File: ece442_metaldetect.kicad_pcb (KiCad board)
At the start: 2 copper layers, 35 parts, among them J4 Conn_01x08_Male, M1 Motor_DC, U4 74LS86

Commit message: Add files via upload
the actual changes made
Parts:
- removed C11: 100n, Capacitor_SMD:C_0402_1005Metric
- added J1: 1-2834011-2, TestPoint:connect_detect, F.Cu at (99.1, 104.1)
- added J2: 1-2834011-2, TestPoint:connect_detect, F.Cu at (88.9, 104.1)
- added J3: Conn_01x03_Male, Connector_PinHeader_2.54mm:PinHeader_1x03_P2.54mm_Horizontal, F.Cu at (160.7, 111.8)
- added J5: Screw_Terminal_01x02, Connector_PinHeader_2.54mm:PinHeader_1x02_P2.54mm_Vertical, F.Cu at (114.3, 104.1)
- added J6: Screw_Terminal_01x02, Connector_PinHeader_2.54mm:PinHeader_1x02_P2.54mm_Vertical, F.Cu at (104.1, 121.9)
- added U1: LM1458N, TestPoint:DIP794-detect, B.Cu at (109.2, 114.3)
- added U2: LMC6032IMX/NOPB, TestPoint:SOIC127P599X175-8N, B.Cu at (142.2, 116.8)
- added U3: LMC6032IMX/NOPB, TestPoint:SOIC127P599X175-8N, B.Cu at (128.3, 111.8)
- C1, C2, D1, D2, R1, R10, R11, R12, R13, R14, R15, R16, R2, R3, R4, R5, R6, R7, R8, R9, U4: moved to B.Cu
- C10, C12, C3, C4, C5, C6, C7, C8, C9: footprint Capacitor_SMD:C_0402_1005Metric -> Capacitor_SMD:C_0805_2012Metric; moved to B.Cu
- M1: footprint libraries:VCLP0820B004L_Vibrator -> TestPoint:vclp_vibrator
- moved C10 64.7 mm to (101.6, 114.3), turned to -90 degrees
- moved J4 57.2 mm to (83.1, 123.2), turned to 180 degrees
- moved C7 56.9 mm to (88.9, 109.2), turned to -90 degrees
- moved M1 51.9 mm to (96.5, 116.8)
- moved R9 51.0 mm to (109.2, 116.8), turned to -90 degrees
- moved A1 46.7 mm to (114.3, 121.9), turned to 90 degrees
- moved R4 46.3 mm to (99.1, 109.2), turned to 180 degrees
- moved R15 45.5 mm to (116.8, 119.4), turned to 180 degrees
- moved D2 45.3 mm to (123.2, 116.8), turned to 180 degrees
- moved C1 39.9 mm to (91.4, 121.9), turned to 180 degrees
- moved C9 38.4 mm to (134.6, 116.8), turned to -90 degrees
- moved C8 36.2 mm to (137.2, 116.8), turned to 90 degrees
- moved R2 36.1 mm to (121.9, 114.3), turned to 180 degrees
- moved R12 32.8 mm to (144.8, 111.8), turned to 90 degrees
- moved U4 32.6 mm to (151.1, 114.3), turned to 90 degrees
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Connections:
- A1 pad 27: unconnected-(A1-Pad27) -> +5V
- A1 pad 29: unconnected-(A1-Pad29) -> GND
- A1 pad 4: unconnected-(A1-Pad4) -> GND
- C10 pad 1: unconnected-(C10-Pad1) -> +12V
- C10 pad 2: unconnected-(C10-Pad2) -> GND
- C12 pad 1: unconnected-(C12-Pad1) -> +5V
- C12 pad 2: unconnected-(C12-Pad2) -> GND
- C5 pad 1: unconnected-(C5-Pad1) -> +9V
- C5 pad 2: unconnected-(C5-Pad2) -> GND
- C6 pad 1: unconnected-(C6-Pad1) -> +12V
- C6 pad 2: unconnected-(C6-Pad2) -> GND
- C7 pad 1: unconnected-(C7-Pad1) -> +12V
- C7 pad 2: unconnected-(C7-Pad2) -> GND
- C8 pad 1: unconnected-(C8-Pad1) -> GND
- C8 pad 2: unconnected-(C8-Pad2) -> +5V
- C9 pad 1: unconnected-(C9-Pad1) -> +5V
- C9 pad 2: unconnected-(C9-Pad2) -> GND
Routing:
- net GND: track 0.00 -> 259.0 mm, vias 0 -> 10
- net /ReferenceSignalSquare: track 0.00 -> 123.9 mm
- net +5V: track 0.00 -> 121.9 mm, vias 0 -> 3
- net /Sin12.0Vpp: track 0.00 -> 121.5 mm, vias 0 -> 3
- net /rxSignalSquare: track 0.00 -> 103.6 mm, vias 0 -> 2
- net /PhaseShiftSquareWave: track 0.00 -> 94.0 mm, vias 0 -> 5
- net /RXSinWave: track 0.00 -> 93.3 mm, vias 0 -> 3
- net +12V: track 0.00 -> 74.2 mm, vias 0 -> 5
- net GNDREF: track 0.00 -> 58.8 mm, vias 0 -> 6
- net +9V: track 0.00 -> 41.3 mm, vias 0 -> 1
- net /OP1IN+2: track 0.00 -> 35.1 mm
- net Net-(C4-Pad2): track 0.00 -> 25.3 mm, vias 0 -> 2
- net /OP1IN-2: track 0.00 -> 23.6 mm
- net /Sin1.4Vpp: track 0.00 -> 22.1 mm, vias 0 -> 2
- net Net-(M1-Pad1): track 0.00 -> 16.4 mm, vias 0 -> 1
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- added copper zone on B.Cu, net GND
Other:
- board outline added: 81.3 x 25.4 mm

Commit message: Add files via upload
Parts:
- moved J5 5.08 mm to (109.2, 104.1)
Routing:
- net GND: track 259.0 -> 253.7 mm
- net +9V: track 41.3 -> 39.6 mm
- removed copper zone on B.Cu, net GND
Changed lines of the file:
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@@
     (property "Sheetname" "")
     (attr through_hole)
-    (fp_text reference "J4" (at 4.385 -2.27) (layer "F.SilkS")
+    (fp_text reference "J4" (at -0.705 -2.27) (layer "F.SilkS")
       (effects (font (size 1 1) (thickness 0.15)))
     )
@@
     (property "Sheetname" "")
     (attr through_hole)
-    (fp_text reference "J3" (at 4.385 -2.27) (layer "F.SilkS")
+    (fp_text reference "J3" (at -0.705 -2.54) (layer "F.SilkS")
       (effects (font (size 1 1) (thickness 0.15)))
     )
@@
     (property "Sheetname" "")
     (attr through_hole)
-    (fp_text reference "A1" (at 5.08 40.64 90) (layer "B.SilkS")
+    (fp_text reference "A1" (at -0.01 40.64 180) (layer "B.SilkS")
       (effects (font (size 1 1) (thickness 0.15)) (justify mirror))
     )
@@
       (effects (font (size 1 1) (thickness 0.15)))
     )
-    (fp_text user "${REFERENCE}" (at 6.35 36.83) (layer "F.Fab")
+    (fp_text user "${REFERENCE}" (at -1.27 40.64) (layer "F.Fab")
       (effects (font (size 1 1) (thickness 0.15)))
     )
@@
   )
   (footprint "Connector_PinHeader_2.54mm:PinHeader_1x02_P2.54mm_Vertical" (layer "F.Cu")
-    (at 114.3 104.14 90)
+    (at 109.22 104.14 90)
     (descr "Through hole straight pin header, 1x02, 2.54mm pitch, single row")
     (tags "Through hole pin header THT 1x02 2.54mm single row")
@@
       (effects (font (size 1 1) (thickness 0.15)))
     )
-    (fp_text user "${REFERENCE}" (at 0 1.27) (layer "F.Fab")
+    (fp_text user "${REFERENCE}" (at -2.54 1.27) (layer "F.Fab")
       (effects (font (size 1 1) (thickness 0.15)))
     )
@@
     (property "Sheetname" "")
     (attr smd)
-    (fp_text reference "C12" (at 0 1.68) (layer "B.SilkS")
+    (fp_text reference "C12" (at 2.54 0) (layer "B.SilkS")
       (effects (font (size 1 1) (thickness 0.15)) (justify mirror))
     )
@@
     (property "Sheetname" "")
     (attr smd)
-    (fp_text reference "R2" (at 0 1.43) (layer "B.SilkS")
+    (fp_text reference "R2" (at -2.54 0) (layer "B.SilkS")
       (effects (font (size 1 1) (thickness 0.15)) (justify mirror))
     )
@@
     (property "Sheetname" "")
     (attr smd)
-    (fp_text reference "R4" (at 0 1.82) (layer "B.SilkS")
+    (fp_text reference "R4" (at -2.54 1.82) (layer "B.SilkS")
       (effects (font (size 1 1) (thickness 0.15)) (justify mirror))
     )
@@
     (property "Sheetname" "")
     (attr smd)
-    (fp_text reference "C5" (at 0 1.68 90) (layer "B.SilkS")
+    (fp_text reference "C5" (at -0.261252 -2.54 90) (layer "B.SilkS")
       (effects (font (size 1 1) (thickness 0.15)) (justify mirror))
     )
@@
     (property "Sheetname" "")
     (attr smd)
-    (fp_text reference "C8" (at 0 1.68 90) (layer "B.SilkS")
+    (fp_text reference "C8" (at 2.54 0 90) (layer "B.SilkS")
       (effects (font (size 1 1) (thickness 0.15)) (justify mirror))
     )
@@
     (property "Sheetname" "")
     (attr smd)
-    (fp_text reference "R8" (at 0 1.65 90) (layer "B.SilkS")
+    (fp_text reference "R8" (at -2.54 0 90) (layer "B.SilkS")
       (effects (font (size 1 1) (thickness 0.15)) (justify mirror))
     )
@@
     (property "Sheetname" "")
     (attr smd)
-    (fp_text reference "R7" (at 0 1.82 90) (layer "B.SilkS")
+    (fp_text reference "R7" (at 2.54 1.82 90) (layer "B.SilkS")
       (effects (font (size 1 1) (thickness 0.15)) (justify mirror))
     )
@@
     (property "Sheetname" "")
     (attr smd)
-    (fp_text reference "R12" (at 0 1.65 90) (layer "B.SilkS")
+    (fp_text reference "R12" (at 2.54 2.54 90) (layer "B.SilkS")
       (effects (font (size 1 1) (thickness 0.15)) (justify mirror))
     )
@@
     (property "Sheetname" "")
     (attr smd)
-    (fp_text reference "R14" (at 0 1.65) (layer "B.SilkS")
+    (fp_text reference "R14" (at 2.54 0) (layer "B.SilkS")
       (effects (font (size 1 1) (thickness 0.15)) (justify mirror))
     )
@@
     (property "Sheetname" "")
     (attr through_hole)
-    (fp_text reference "C1" (at 2.5 3) (layer "B.SilkS")
+    (fp_text reference "C1" (at 2.5 -2.54) (layer "B.SilkS")
       (effects (font (size 1 1) (thickness 0.15)) (justify mirror))
     )
@@
     (property "Sheetname" "")
     (attr smd)
-    (fp_text reference "R3" (at 0 1.82) (layer "B.SilkS")
+    (fp_text reference "R3" (at -3.6175 0) (layer "B.SilkS")
       (effects (font (size 1 1) (thickness 0.15)) (justify mirror))
     )
@@
     (property "Sheetname" "")
     (attr smd)
-    (fp_text reference "C9" (at 0 1.68 90) (layer "B.SilkS")
+    (fp_text reference "C9" (at 2.54 0 90) (layer "B.SilkS")
       (effects (font (size 1 1) (thickness 0.15)) (justify mirror))
     )
@@
     (property "Sheetname" "")
     (attr smd)
-    (fp_text reference "R1" (at 0 1.65) (layer "B.SilkS")
+    (fp_text reference "R1" (at 4.1675 0) (layer "B.SilkS")
       (effects (font (size 1 1) (thickness 0.15)) (justify mirror))
     )
@@
     (property "Sheetname" "")
     (attr smd)
-    (fp_text reference "R11" (at 0 1.65 90) (layer "B.SilkS")
+    (fp_text reference "R11" (at 2.54 0 90) (layer "B.SilkS")
       (effects (font (size 1 1) (thickness 0.15)) (justify mirror))
     )
@@
     (property "Sheetname" "")
     (attr smd)
-    (fp_text reference "C3" (at 0 1.68 90) (layer "B.SilkS")
+    (fp_text reference "C3" (at 2.54 0) (layer "B.SilkS")
       (effects (font (size 1 1) (thickness 0.15)) (justify mirror))
     )
@@
     (property "Sheetname" "")
     (attr smd)
-    (fp_text reference "C6" (at 0 1.68 90) (layer "B.SilkS")
+    (fp_text reference "C6" (at -2.54 0 90) (layer "B.SilkS")
       (effects (font (size 1 1) (thickness 0.15)) (justify mirror))
     )
@@
     (property "Sheetname" "")
     (attr through_hole)
-    (fp_text reference "U1" (at -3.105 4.872) (layer "B.SilkS")
+    (fp_text reference "U1" (at 0 5.08) (layer "B.SilkS")
       (effects (font (size 1 1) (thickness 0.15)) (justify mirror))
     )
@@
     (property "Sheetname" "")
     (attr smd)
-    (fp_text reference "U2" (at -0.385 3.537) (layer "B.SilkS")
+    (fp_text reference "U2" (at -5.08 -2.54) (layer "B.SilkS")
       (effects (font (size 1 1) (thickness 0.15)) (justify mirror))
     )
@@
     (property "Sheetname" "")
     (attr smd)
-    (fp_text reference "R15" (at 0 1.65) (layer "B.SilkS")
+    (fp_text reference "R15" (at -5.08 0) (layer "B.SilkS")
       (effects (font (size 1 1) (thickness 0.15)) (justify mirror))
     )
@@
   (segment (start 81.940489 124.349511) (end 84.465958 126.87498) (width 0.25) (layer "F.Cu") (net 4))
   (segment (start 99.18502 126.87498) (end 101.6 124.46) (width 0.25) (layer "F.Cu") (net 4))
-  (segment (start 116.84 106.67) (end 116.84 104.14) (width 0.25) (layer "F.Cu") (net 4))
   (segment (start 137.16 118.6555) (end 138.3968 119.8923) (width 0.25) (layer "F.Cu") (net 4))
   (segment (start 84.465958 126.87498) (end 99.18502 126.87498) (width 0.25) (layer "F.Cu") (net 4))
@@
   (segment (start 145.35 118.745) (end 144.71 118.745) (width 0.25) (layer "B.Cu") (net 4))
   (segment (start 107.085401 112.71) (end 105.473863 114.321538) (width 0.25) (layer "B.Cu") (net 4))
+  (segment (start 116.84 104.14) (end 111.76 104.14) (width 0.25) (layer "B.Cu") (net 4))
   (segment (start 161.899511 110.585489) (end 161.899511 113.125489) (width 0.25) (layer "B.Cu") (net 4))
   (segment (start 159.481206 110.585489) (end 161.899511 110.585489) (width 0.25) (layer "B.Cu") (net 4))
-  (segment (start 115.665489 102.965489) (end 106.904511 102.965489) (width 0.25) (layer "B.Cu") (net 4))
   (segment (start 105.73 104.14) (end 104.14 104.14) (width 0.25) (layer "B.Cu") (net 4))
   (segment (start 118.43 109.22) (end 116.84 109.22) (width 0.25) (layer "B.Cu") (net 4))
@@
   (segment (start 89.73 109.34) (end 88.9 110.17) (width 0.25) (layer "B.Cu") (net 4))
   (segment (start 109.22 112.71) (end 107.085401 112.71) (width 0.25) (layer "B.Cu") (net 4))
+  (segment (start 116.84 106.67) (end 116.84 104.14) (width 0.25) (layer "B.Cu") (net 4))
   (segment (start 137.16 117.79) (end 137.16 118.6555) (width 0.25) (layer "B.Cu") (net 4))
-  (segment (start 116.84 104.14) (end 115.665489 102.965489) (width 0.25) (layer "B.Cu") (net 4))
   (segment (start 117.7525 119.38) (end 118.20202 119.82952) (width 0.25) (layer "B.Cu") (net 5))
   (segment (start 118.20202 119.82952) (end 122.37952 119.82952) (width 0.25) (layer "B.Cu") (net 5))
@@
   (segment (start 95.377483 118.095) (end 104.177299 109.295184) (width 0.25) (layer "F.Cu") (net 29))
   (segment (start 83.115 118.095) (end 95.377483 118.095) (width 0.25) (layer "F.Cu") (net 29))
-  (segment (start 114.3 106.67) (end 114.3 104.14) (width 0.25) (layer "F.Cu") (net 29))
   (via (at 104.177299 106.642701) (size 0.8) (drill 0.4) (layers "F.Cu" "B.Cu") (net 29))
-  (segment (start 112.72 105.09) (end 114.3 106.67) (width 0.25) (layer "B.Cu") (net 29))
-  (segment (start 106.68 105.09) (end 112.72 105.09) (width 0.25) (layer "B.Cu") (net 29))
+  (segment (start 107.63 104.14) (end 109.22 104.14) (width 0.25) (layer "B.Cu") (net 29))
+  (segment (start 114.3 106.67) (end 111.75 106.67) (width 0.25) (layer "B.Cu") (net 29))
+  (segment (start 106.68 105.09) (end 107.63 104.14) (width 0.25) (layer "B.Cu") (net 29))
+  (segment (start 111.75 106.67) (end 109.22 104.14) (width 0.25) (layer "B.Cu") (net 29))
   (segment (start 104.177299 106.642701) (end 105.73 105.09) (width 0.25) (layer "B.Cu") (net 29))
   (segment (start 105.73 105.09) (end 106.68 105.09) (width 0.25) (layer "B.Cu") (net 29))
@@
   (segment (start 105.25 115.57) (end 106.52 114.3) (width 0.25) (layer "B.Cu") (net 49))
   (segment (start 109.38 114.3) (end 113.19 110.49) (width 0.25) (layer "B.Cu") (net 49))
-  (zone (net 4) (net_name "GND") (layer "B.Cu") (hatch edge 0.508)
-    (connect_pads (clearance 0.508))
-    (min_thickness 0.254) (filled_areas_thickness no)
-    (fill yes (thermal_gap 0.508) (thermal_bridge_width 0.508))
-    (polygon
-      (pts
-        (xy 162.56 127)
-        (xy 81.28 127)
-        (xy 81.28 101.6)
-        (xy 162.56 101.6)
-      )
-    )
-  )
 )

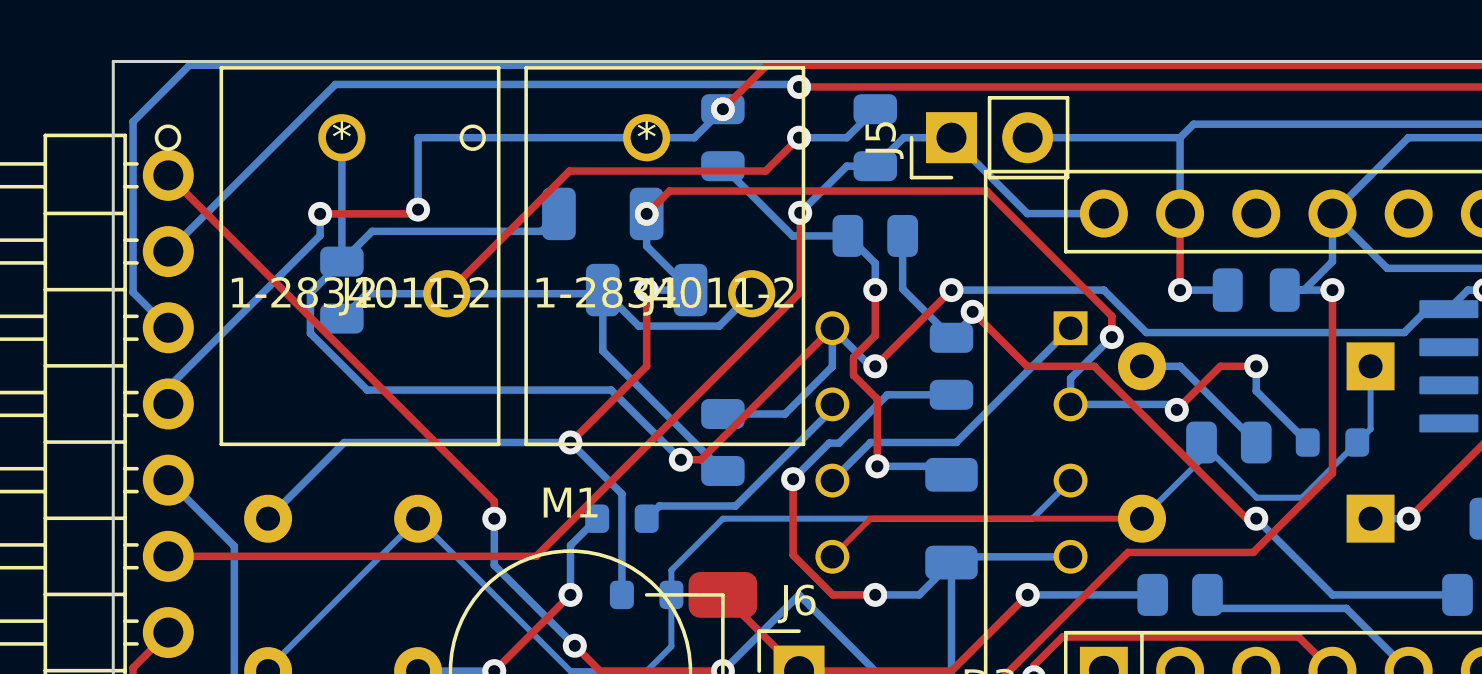
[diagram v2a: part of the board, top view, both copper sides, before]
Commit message: moved j5 and slikscreen labels to be more clear
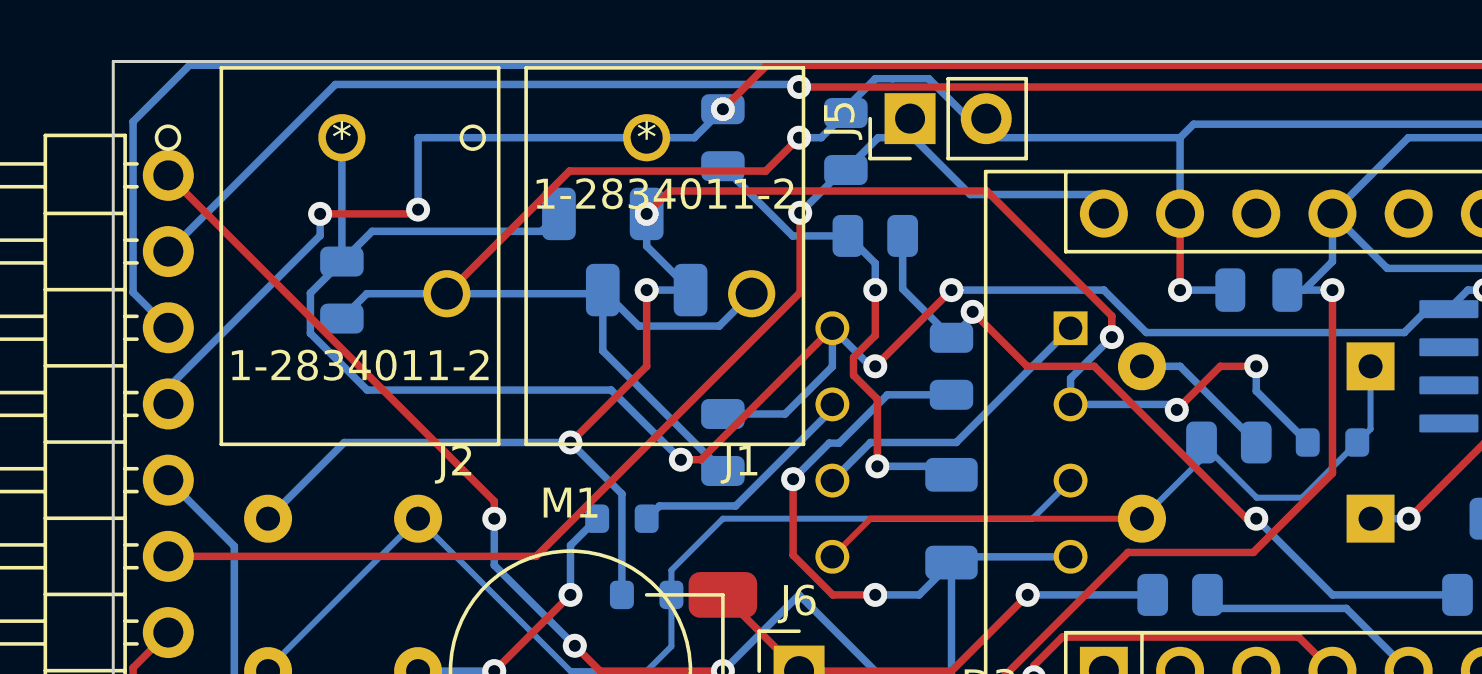
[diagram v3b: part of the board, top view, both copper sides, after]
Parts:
- moved J5 1.52 mm to (107.8, 103.5)
- moved C5 0.99 mm to (105.7, 104.3)
- moved C12 0.09 mm to (119.5, 109.2)
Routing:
- net GND: track 253.7 -> 259.8 mm
